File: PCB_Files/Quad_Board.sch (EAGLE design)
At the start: 35 parts

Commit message: Updates in PCB Schematic and Layout
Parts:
- added GPIO_EXTRA: (no value), pinhead:PINHD-1X5
- added R1: (no value), resistor:R-EU_M1206
- added U$3: TXS0102, TXS0102-bi-directional-translator:TXS0102
- R4, R5, R6: device eagle-ltspice:RR2512 -> resistor:R-EU_M1206
- R7: device rcl:R-US_0204/5 -> resistor:R-EU_M1206
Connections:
- new net P4.0_GPIO: GPIO_EXTRA.1, MSP432P401R.P4.0/A13
- new net P4.1_GPIO: GPIO_EXTRA.2, MSP432P401R.P4.1/A12
- new net P4.5_GPIO: GPIO_EXTRA.3, MSP432P401R.P4.5/A8
- new net P4.6_GPIO: GPIO_EXTRA.4, MSP432P401R.P4.6/A7
- new net P4.7_GPIO: GPIO_EXTRA.5, MSP432P401R.P4.7/A6
- new net VBAT_TX: BATTERY_FC_PINS.1, U$3.P$4
- net 3V3: now also R1.1, U$3.P$6, U$3.P$7
- net 5V: now also U$3.P$2
- net GND: now also R1.2, U$3.P$3
- net P2.2_RX: now also U$3.P$5; no longer BATTERY_FC_PINS.1
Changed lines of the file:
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@@
 <part name="SUPPLY1" library="SparkFun-Aesthetics" deviceset="5V" device=""/>
 <part name="SUPPLY2" library="SparkFun-Aesthetics" deviceset="3.3V" device=""/>
-<part name="R4" library="eagle-ltspice" deviceset="R" device="R2512" value="100k"/>
+<part name="R4" library="resistor" deviceset="R-EU_" device="M1206" value="100k"/>
 <part name="LEVEL_TRANSLATOR_2" library="SparkFun-DigitalIC" deviceset="TXB0104PWR" device="SOIC14"/>
 <part name="SUPPLY3" library="SparkFun-Aesthetics" deviceset="5V" device=""/>
 <part name="SUPPLY4" library="SparkFun-Aesthetics" deviceset="3.3V" device=""/>
-<part name="R5" library="eagle-ltspice" deviceset="R" device="R2512" value="100k"/>
+<part name="R5" library="resistor" deviceset="R-EU_" device="M1206" value="100k"/>
 <part name="LEVEL_TRANSLATOR_3" library="SparkFun-DigitalIC" deviceset="TXB0104PWR" device="SOIC14"/>
 <part name="SUPPLY5" library="SparkFun-Aesthetics" deviceset="5V" device=""/>
 <part name="SUPPLY6" library="SparkFun-Aesthetics" deviceset="3.3V" device=""/>
-<part name="R6" library="eagle-ltspice" deviceset="R" device="R2512" value="100k"/>
+<part name="R6" library="resistor" deviceset="R-EU_" device="M1206" value="100k"/>
 <part name="FRAME1" library="frames" deviceset="FRAME_D_L" device=""/>
 <part name="U$1" library="TXS0102-bi-directional-translator" deviceset="TXS0102" device=""/>
-<part name="R7" library="rcl" deviceset="R-US_" device="0204/5"/>
+<part name="R7" library="resistor" deviceset="R-EU_" device="M1206"/>
 <part name="GND2" library="SparkFun-Aesthetics" deviceset="GND" device=""/>
 <part name="GND3" library="SparkFun-Aesthetics" deviceset="GND" device=""/>
@@
 <part name="TP2" library="testpad" deviceset="TP" device="B2,54"/>
 <part name="TP3" library="testpad" deviceset="TP" device="B1,27"/>
+<part name="U$3" library="TXS0102-bi-directional-translator" deviceset="TXS0102" device=""/>
+<part name="R1" library="resistor" deviceset="R-EU_" device="M1206"/>
+<part name="GND1" library="SparkFun-Aesthetics" deviceset="GND" device=""/>
+<part name="GPIO_EXTRA" library="pinhead" deviceset="PINHD-1X5" device=""/>
 </parts>
 <sheets>
@@
 <instance part="GND5" gate="1" x="73.66" y="-42.164"/>
 <instance part="GND6" gate="1" x="-385.572" y="152.4"/>
-<instance part="GND7" gate="1" x="-319.786" y="4.572"/>
+<instance part="GND7" gate="1" x="-321.818" y="7.874"/>
 <instance part="GND8" gate="1" x="-416.814" y="16.002"/>
 <instance part="GND9" gate="1" x="-414.02" y="-12.7"/>
@@
 <instance part="TP2" gate="G$1" x="-281.94" y="7.62"/>
 <instance part="TP3" gate="G$1" x="-331.47" y="179.07" rot="R90"/>
+<instance part="U$3" gate="G$1" x="-383.54" y="-7.62"/>
+<instance part="R1" gate="G$1" x="-361.95" y="-10.16"/>
+<instance part="GND1" gate="1" x="-352.552" y="-12.7"/>
+<instance part="GPIO_EXTRA" gate="A" x="-350.52" y="127" rot="MR0"/>
 </instances>
 <busses>
@@
 <segment>
 <pinref part="5V_PDB" gate="G$1" pin="2"/>
-<wire x1="-310.134" y1="10.414" x2="-319.786" y2="10.414" width="0.1524" layer="91"/>
-<wire x1="-319.786" y1="10.414" x2="-319.786" y2="7.112" width="0.1524" layer="91"/>
+<wire x1="-310.134" y1="10.414" x2="-321.818" y2="10.414" width="0.1524" layer="91"/>
 <pinref part="GND7" gate="1" pin="GND"/>
 </segment>
@@
 <wire x1="-281.94" y1="2.54" x2="-276.86" y2="2.54" width="0.1524" layer="91"/>
 <label x="-274.32" y="0" size="1.27" layer="95" xref="yes"/>
+</segment>
+<segment>
+<pinref part="R1" gate="G$1" pin="2"/>
+<wire x1="-356.87" y1="-10.16" x2="-352.552" y2="-10.16" width="0.1524" layer="91"/>
+<pinref part="GND1" gate="1" pin="GND"/>
+</segment>
+<segment>
+<pinref part="U$3" gate="G$1" pin="P$3"/>
+<wire x1="-391.16" y1="-10.16" x2="-396.24" y2="-10.16" width="0.1524" layer="91"/>
+<label x="-396.24" y="-12.7" size="1.27" layer="95" xref="yes"/>
 </segment>
 </net>
@@
 <wire x1="-429.26" y1="43.18" x2="-415.544" y2="43.18" width="0.1524" layer="91"/>
 <label x="-424.18" y="48.26" size="1.778" layer="95"/>
-<label x="-411.48" y="43.18" size="1.778" layer="95"/>
 </segment>
 </net>
@@
 <wire x1="-429.26" y1="40.64" x2="-412.242" y2="40.64" width="0.1524" layer="91"/>
 <wire x1="-412.242" y1="40.64" x2="-412.242" y2="46.228" width="0.1524" layer="91"/>
-<label x="-411.48" y="38.1" size="1.778" layer="95"/>
+<label x="-411.48" y="43.18" size="1.778" layer="95"/>
 </segment>
 </net>
@@
 <wire x1="-410.21" y1="38.1" x2="-429.26" y2="38.1" width="0.1524" layer="91"/>
 <pinref part="NAZE32_PINHEAD" gate="A" pin="7"/>
+<label x="-406.4" y="38.1" size="1.27" layer="95" xref="yes"/>
 </segment>
 </net>
@@
 <wire x1="-429.26" y1="33.02" x2="-406.4" y2="33.02" width="0.1524" layer="91"/>
 <wire x1="-406.4" y1="33.02" x2="-406.4" y2="30.988" width="0.1524" layer="91"/>
-<label x="-398.78" y="33.02" size="1.778" layer="95"/>
+<label x="-396.24" y="33.02" size="1.778" layer="95"/>
 </segment>
 </net>
@@
 <label x="-401.32" y="160.02" size="1.27" layer="95" xref="yes"/>
 </segment>
+<segment>
+<pinref part="U$3" gate="G$1" pin="P$7"/>
+<wire x1="-375.92" y1="-5.08" x2="-373.38" y2="-5.08" width="0.1524" layer="91"/>
+<label x="-370.84" y="-2.54" size="1.778" layer="95" rot="R180"/>
+</segment>
+<segment>
+<pinref part="U$3" gate="G$1" pin="P$6"/>
+<label x="-370.84" y="-7.62" size="1.778" layer="95" rot="R180"/>
+<wire x1="-375.92" y1="-10.16" x2="-370.84" y2="-10.16" width="0.1524" layer="91"/>
+<pinref part="R1" gate="G$1" pin="1"/>
+<wire x1="-370.84" y1="-10.16" x2="-367.03" y2="-10.16" width="0.1524" layer="91"/>
+<wire x1="-370.84" y1="-10.16" x2="-370.84" y2="-7.62" width="0.1524" layer="91"/>
+<junction x="-370.84" y="-10.16"/>
+<label x="-368.3" y="-5.08" size="1.27" layer="95" xref="yes"/>
+</segment>
 </net>
 <net name="N$2" class="0">
@@
 <label x="-424.18" y="157.48" size="1.778" layer="95" rot="R180"/>
 </segment>
+<segment>
+<pinref part="U$3" gate="G$1" pin="P$2"/>
+<wire x1="-391.16" y1="-5.08" x2="-398.78" y2="-5.08" width="0.1524" layer="91"/>
+<label x="-396.24" y="-7.62" size="1.27" layer="95" xref="yes"/>
+</segment>
 </net>
 <net name="P5.6_5V" class="0">
@@
 </segment>
 <segment>
+<pinref part="U$3" gate="G$1" pin="P$5"/>
+<label x="-369.824" y="-12.7" size="1.778" layer="95" rot="R180"/>
+<wire x1="-375.92" y1="-15.24" x2="-331.978" y2="-15.24" width="0.1524" layer="91"/>
+<label x="-368.3" y="-17.78" size="1.27" layer="95" xref="yes"/>
+</segment>
+</net>
+<net name="P4.0_GPIO" class="0">
+<segment>
+<pinref part="MSP432P401R" gate="MSP432" pin="P4.0/A13"/>
+<wire x1="-306.07" y1="138.43" x2="-318.262" y2="138.43" width="0.1524" layer="91"/>
+<label x="-325.12" y="139.7" size="1.27" layer="95" xref="yes"/>
+</segment>
+<segment>
+<pinref part="GPIO_EXTRA" gate="A" pin="1"/>
+<wire x1="-347.98" y1="132.08" x2="-337.82" y2="132.08" width="0.1524" layer="91"/>
+</segment>
+</net>
+<net name="P4.1_GPIO" class="0">
+<segment>
+<pinref part="MSP432P401R" gate="MSP432" pin="P4.1/A12"/>
+<wire x1="-306.07" y1="135.89" x2="-318.008" y2="135.89" width="0.1524" layer="91"/>
+<label x="-325.12" y="137.16" size="1.27" layer="95" xref="yes"/>
+</segment>
+<segment>
+<pinref part="GPIO_EXTRA" gate="A" pin="2"/>
+<wire x1="-347.98" y1="129.54" x2="-337.82" y2="129.54" width="0.1524" layer="91"/>
+</segment>
+</net>
+<net name="P4.5_GPIO" class="0">
+<segment>
+<pinref part="MSP432P401R" gate="MSP432" pin="P4.5/A8"/>
+<wire x1="-306.07" y1="125.73" x2="-315.722" y2="125.73" width="0.1524" layer="91"/>
+<label x="-325.12" y="127" size="1.27" layer="95" xref="yes"/>
+</segment>
+<segment>
+<pinref part="GPIO_EXTRA" gate="A" pin="3"/>
+<wire x1="-347.98" y1="127" x2="-337.82" y2="127" width="0.1524" layer="91"/>
+</segment>
+</net>
+<net name="P4.6_GPIO" class="0">
+<segment>
+<pinref part="MSP432P401R" gate="MSP432" pin="P4.6/A7"/>
+<wire x1="-306.07" y1="123.19" x2="-316.484" y2="123.19" width="0.1524" layer="91"/>
+<label x="-325.12" y="124.46" size="1.27" layer="95" xref="yes"/>
+</segment>
+<segment>
+<pinref part="GPIO_EXTRA" gate="A" pin="4"/>
+<wire x1="-347.98" y1="124.46" x2="-337.82" y2="124.46" width="0.1524" layer="91"/>
+</segment>
+</net>
+<net name="VBAT_TX" class="0">
+<segment>
+<pinref part="U$3" gate="G$1" pin="P$4"/>
+<wire x1="-391.16" y1="-15.24" x2="-398.78" y2="-15.24" width="0.1524" layer="91"/>
+<label x="-398.78" y="-17.78" size="1.27" layer="95" xref="yes"/>
+</segment>
+<segment>
 <wire x1="-431.8" y1="-5.08" x2="-439.42" y2="-5.08" width="0.1524" layer="91"/>
 <label x="-439.42" y="-5.08" size="1.27" layer="95" rot="R180" xref="yes"/>
@@
 </segment>
 </net>
+<net name="P4.7_GPIO" class="0">
+<segment>
+<pinref part="GPIO_EXTRA" gate="A" pin="5"/>
+<wire x1="-347.98" y1="121.92" x2="-337.82" y2="121.92" width="0.1524" layer="91"/>
+</segment>
+<segment>
+<pinref part="MSP432P401R" gate="MSP432" pin="P4.7/A6"/>
+<wire x1="-306.07" y1="120.65" x2="-315.722" y2="120.65" width="0.1524" layer="91"/>
+<label x="-325.12" y="121.92" size="1.27" layer="95" xref="yes"/>
+</segment>
+</net>

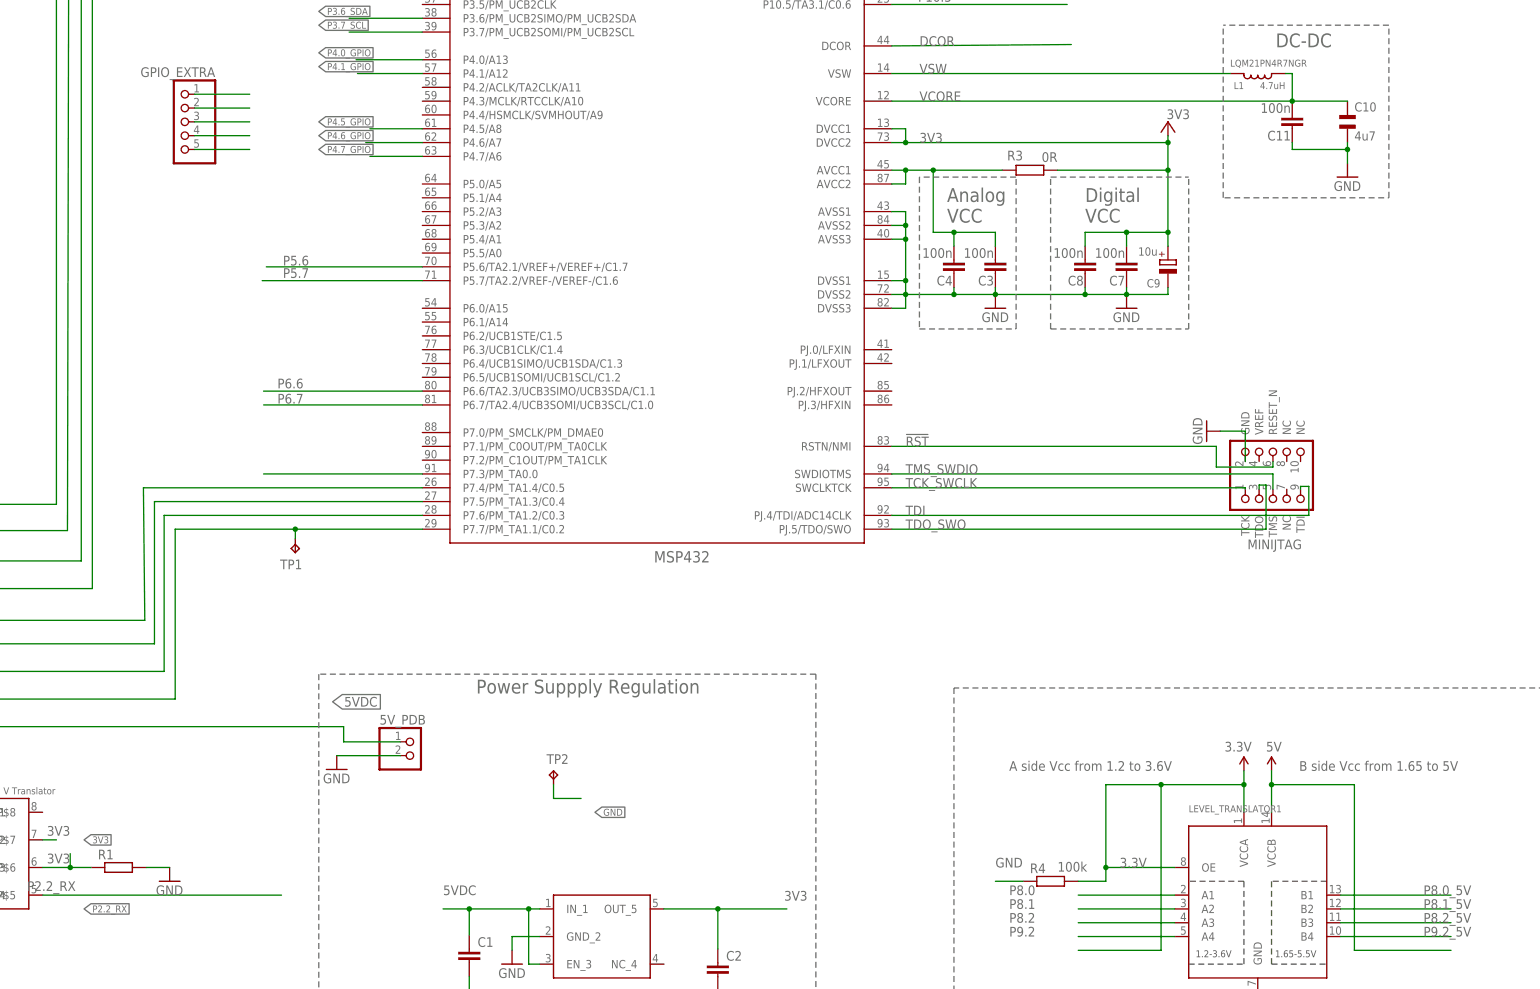
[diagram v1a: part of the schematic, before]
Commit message: Routing almost finalized
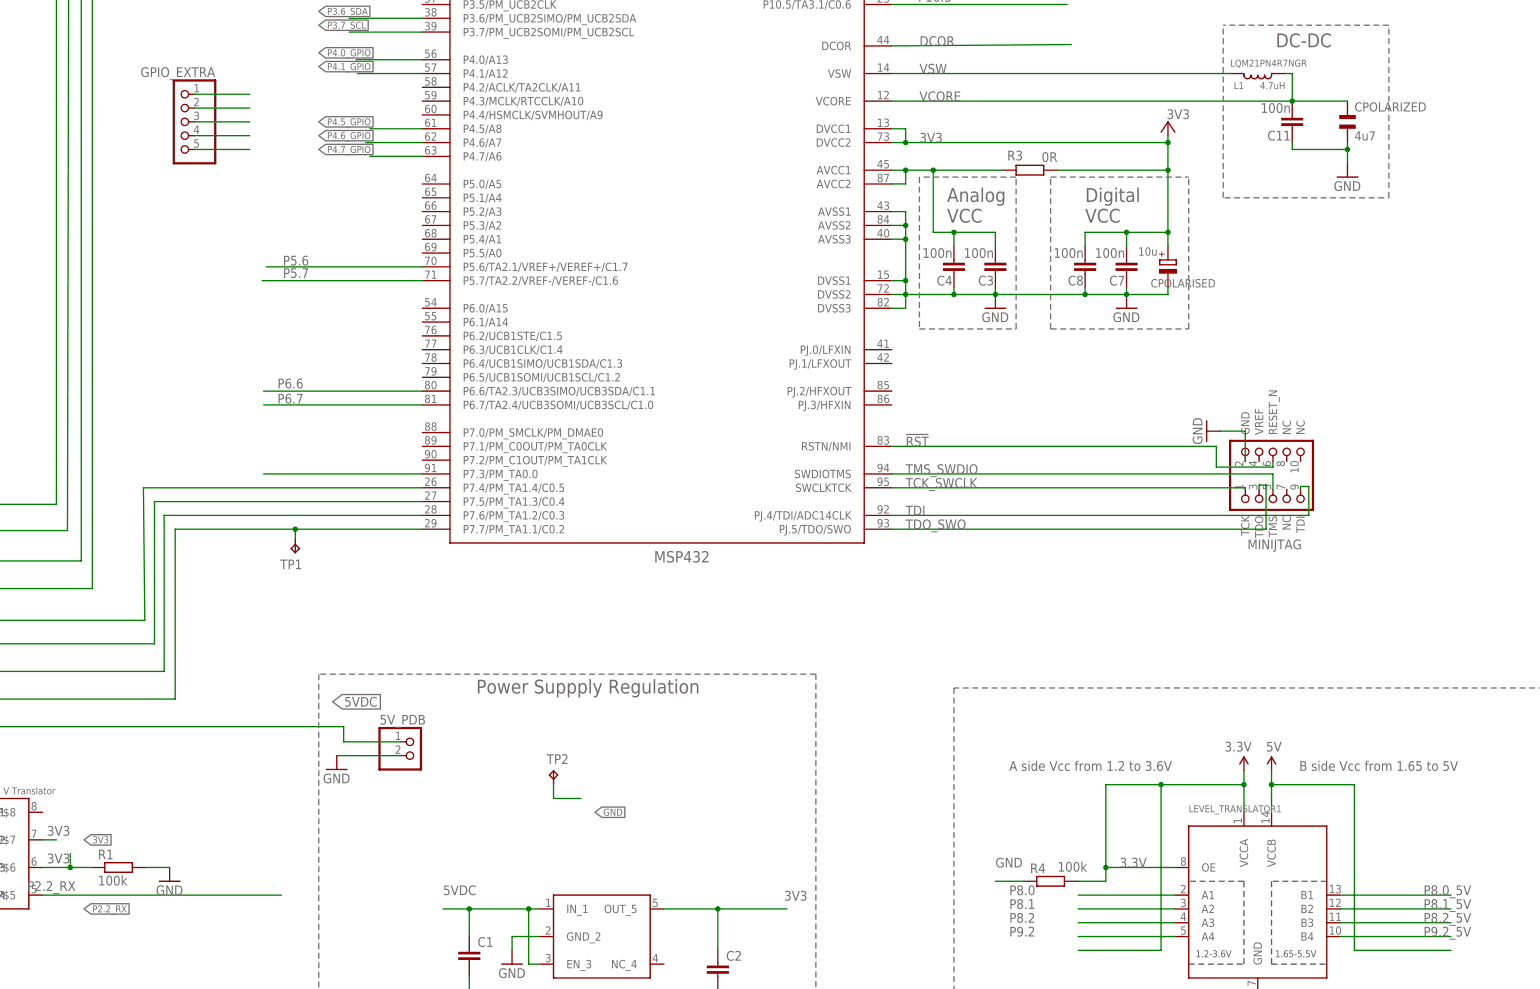
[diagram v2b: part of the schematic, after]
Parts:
- R1: value (none) -> 100k
- renumbered C10 to CPOLARIZED, C9 to CPOLARISED
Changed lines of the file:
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@@
 <?xml version="1.0" encoding="utf-8"?>
 <!DOCTYPE eagle SYSTEM "eagle.dtd">
-<eagle version="6.5.0">
+<eagle version="7.5.0">
 <drawing>
 <settings>
@@
 <part name="C3" library="rcl" deviceset="C-EU" device="C0805" value="100n"/>
 <part name="C4" library="rcl" deviceset="C-EU" device="C0805" value="100n"/>
-<part name="C10" library="cap" deviceset="CSMD0805" device="" value="4u7"/>
+<part name="CPOLARIZED" library="cap" deviceset="CSMD0805" device="" value="4u7"/>
 <part name="L1" library="Murata" deviceset="LQM2MP_G0" device="" value="4.7uH"/>
 <part name="GND41" library="supply1" deviceset="GND" device=""/>
 <part name="C7" library="rcl" deviceset="C-EU" device="C0805" value="100n"/>
 <part name="C8" library="rcl" deviceset="C-EU" device="C0805" value="100n"/>
-<part name="C9" library="rcl" deviceset="CPOL-EU" device="A/3216-18R" value="10u"/>
+<part name="CPOLARISED" library="rcl" deviceset="CPOL-EU" device="A/3216-18R" value="10u"/>
 <part name="R3" library="rcl" deviceset="R-EU_" device="RM0402" value="0R"/>
 <part name="GND44" library="supply1" deviceset="GND" device=""/>
@@
 <part name="TP3" library="testpad" deviceset="TP" device="B1,27"/>
 <part name="U$3" library="TXS0102-bi-directional-translator" deviceset="TXS0102" device=""/>
-<part name="R1" library="resistor" deviceset="R-EU_" device="M1206"/>
+<part name="R1" library="resistor" deviceset="R-EU_" device="M1206" value="100k"/>
 <part name="GND1" library="SparkFun-Aesthetics" deviceset="GND" device=""/>
 <part name="GPIO_EXTRA" library="pinhead" deviceset="PINHD-1X5" device=""/>
@@
 <attribute name="VALUE" x="-208.534" y="103.759" size="1.778" layer="96" rot="R180"/>
 </instance>
-<instance part="C10" gate="G$2" x="-135.89" y="128.27" smashed="yes" rot="R270">
+<instance part="CPOLARIZED" gate="G$2" x="-135.89" y="128.27" smashed="yes" rot="R270">
 <attribute name="NAME" x="-134.62" y="128.905" size="1.6764" layer="95"/>
 <attribute name="VALUE" x="-134.62" y="123.571" size="1.6764" layer="96"/>
@@
 <attribute name="VALUE" x="-184.404" y="103.759" size="1.778" layer="96" rot="R180"/>
 </instance>
-<instance part="C9" gate="G$1" x="-168.91" y="101.6" smashed="yes">
-<attribute name="NAME" x="-170.307" y="98.0694" size="1.524" layer="95" rot="R180"/>
+<instance part="CPOLARISED" gate="G$1" x="-168.91" y="101.6" smashed="yes">
+<attribute name="NAME" x="-160.147" y="98.0694" size="1.524" layer="95" rot="R180"/>
 <attribute name="VALUE" x="-170.815" y="103.9114" size="1.524" layer="96" rot="R180"/>
 </instance>
@@
 <junction x="-184.15" y="95.25"/>
 <wire x1="-176.53" y1="95.25" x2="-168.91" y2="95.25" width="0.1524" layer="91"/>
-<pinref part="C9" gate="G$1" pin="-"/>
+<pinref part="CPOLARISED" gate="G$1" pin="-"/>
 <wire x1="-168.91" y1="96.52" x2="-168.91" y2="95.25" width="0.1524" layer="91"/>
 <wire x1="-200.66" y1="95.25" x2="-184.15" y2="95.25" width="0.1524" layer="91"/>
@@
 <wire x1="-146.05" y1="123.19" x2="-146.05" y2="121.92" width="0.1524" layer="91"/>
 <wire x1="-146.05" y1="121.92" x2="-135.89" y2="121.92" width="0.1524" layer="91"/>
-<pinref part="C10" gate="G$2" pin="2"/>
+<pinref part="CPOLARIZED" gate="G$2" pin="2"/>
 <wire x1="-135.89" y1="123.19" x2="-135.89" y2="121.92" width="0.1524" layer="91"/>
 <junction x="-135.89" y="121.92"/>
@@
 <segment>
 <label x="-214.63" y="130.81" size="1.778" layer="95"/>
-<pinref part="C10" gate="G$2" pin="1"/>
+<pinref part="CPOLARIZED" gate="G$2" pin="1"/>
 <wire x1="-146.05" y1="130.81" x2="-135.89" y2="130.81" width="0.1524" layer="91"/>
 <pinref part="L1" gate="G$1" pin="1"/>
@@
 <segment>
 <wire x1="-189.23" y1="118.11" x2="-168.91" y2="118.11" width="0.1524" layer="91"/>
-<pinref part="C9" gate="G$1" pin="+"/>
+<pinref part="CPOLARISED" gate="G$1" pin="+"/>
 <wire x1="-168.91" y1="118.11" x2="-168.91" y2="106.68" width="0.1524" layer="91"/>
 <pinref part="R3" gate="G$1" pin="1"/>
